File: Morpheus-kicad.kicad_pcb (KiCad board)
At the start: 2 copper layers, 64 parts, among them J1 Conn_02x03_Odd_Even, J2 Conn_02x03_Odd_Even, J3 Conn_02x03_Odd_Even, J4 Conn_02x03_Odd_Even, J5 Conn_02x05_Counter_Clockwise, Q1 IRLZ44N, Q2 IRLB3034PBF, Q3 IRLZ44N, U1 Pololu Driver, U2 Pololu Driver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

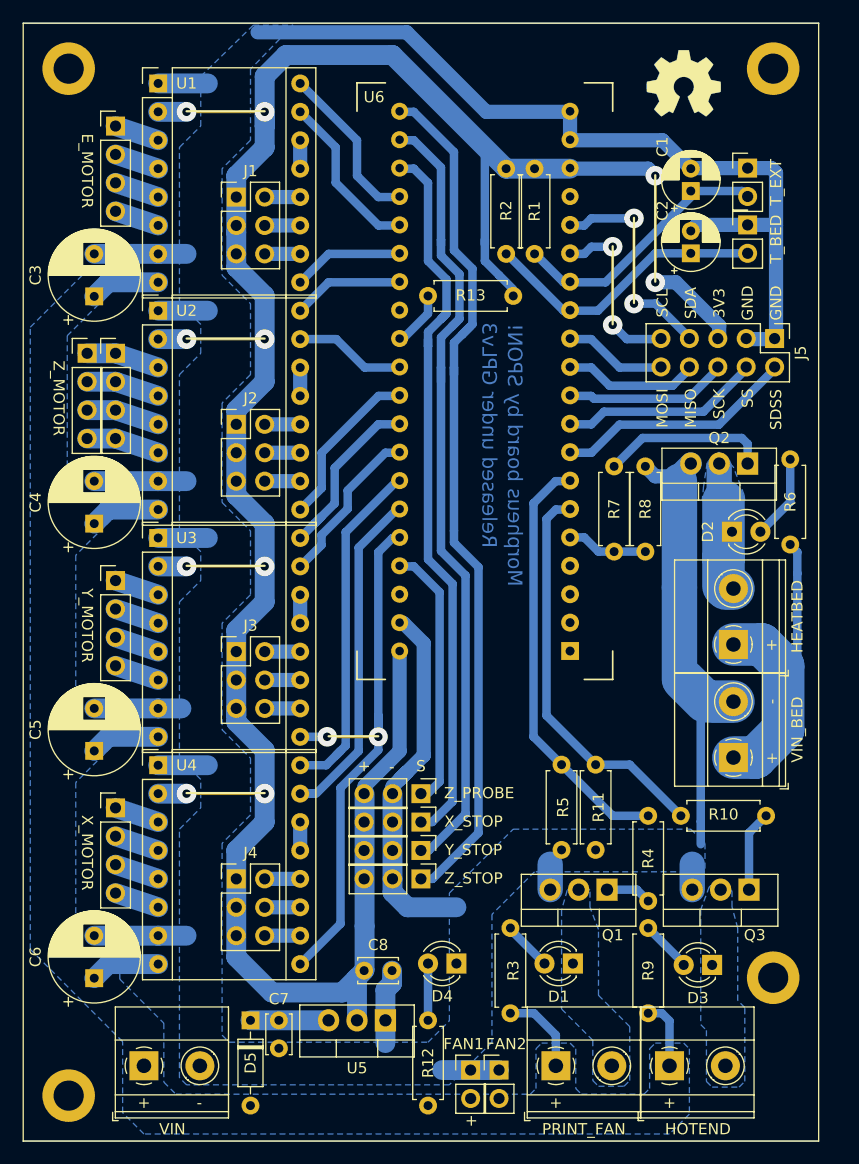
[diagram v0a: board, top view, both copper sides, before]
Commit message: Add reverse current protection
Added a 1N4007 or similar diode to protect from reverse current. Bear in mind that, without a fuse, it will just burn and let current pass again, damaging components.
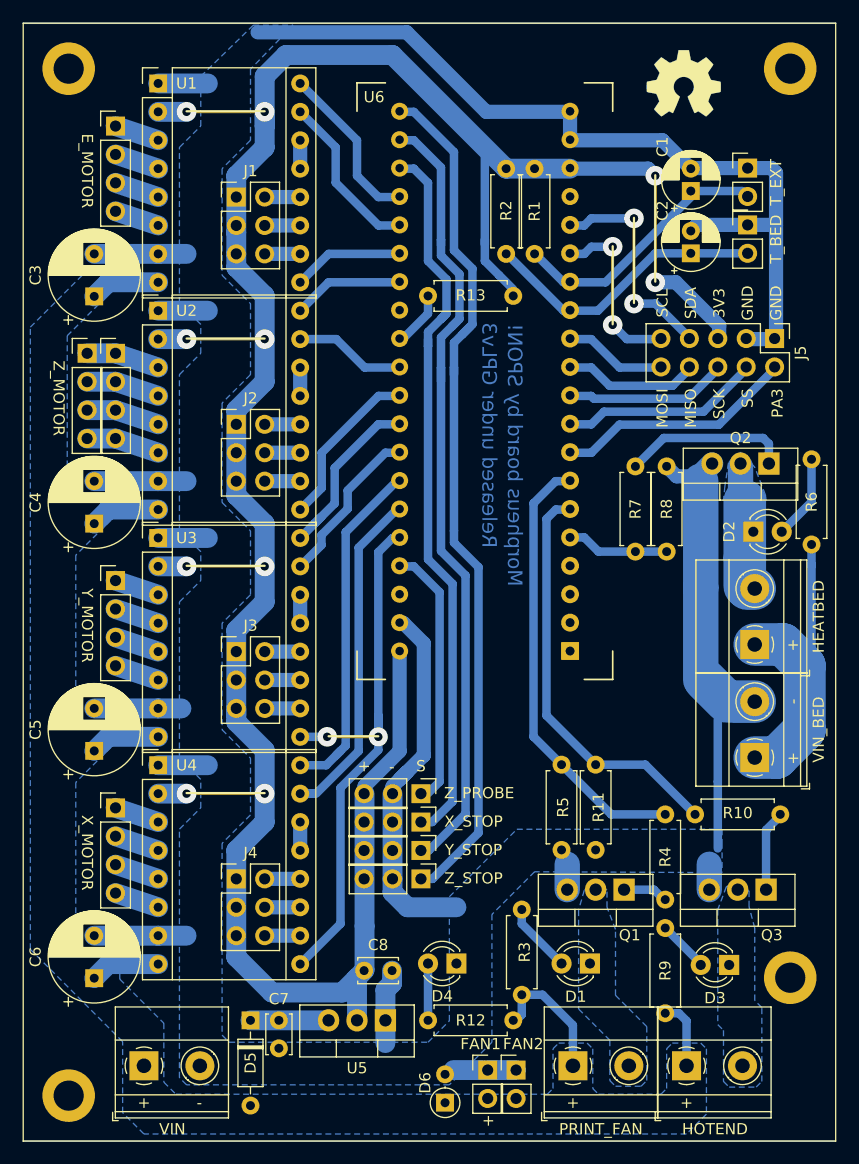
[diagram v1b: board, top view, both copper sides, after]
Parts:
- added D6: 1N4007, Diode_THT:D_DO-35_SOD27_P2.54mm_Vertical_AnodeUp, F.Cu at (73.9, 126.7)
- moved R3 1.94 mm to (80.8, 109.5)
- moved D2 1.91 mm to (101.5, 75.7)
- moved HEATBED1 1.91 mm to (101.6, 85.8)
- moved Q2 1.91 mm to (102.9, 69.6)
- moved R6 1.91 mm to (106.7, 69.2)
- moved R7 1.91 mm to (90.9, 69.8)
- moved R8 1.91 mm to (93.7, 69.8)
- moved VIN_BED1 1.91 mm to (101.6, 95.9)
- moved R4 1.53 mm to (93.6, 108.6)
- moved D1 1.52 mm to (86.9, 114.3)
- moved FAN1 1.52 mm to (77.7, 123.8)
- moved FAN2 1.52 mm to (80.3, 123.8)
- moved HOTEND1 1.52 mm to (95.5, 123.4)
- moved PRINT_FAN1 1.52 mm to (85.3, 123.4)
- moved Q1 1.52 mm to (89.9, 107.7)
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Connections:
- net SDSS renamed PA3
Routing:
- net +12V: track 38.5 -> 43.3 mm
- net (no net): track 142.2 -> 145.3 mm
- net Net-(D1-Pad2): track 4.33 -> 6.30 mm
- net HEATER_BED: track 7.26 -> 9.16 mm
- net PRINT_FAN: track 38.1 -> 39.6 mm
- net HOTEND: track 35.8 -> 37.0 mm
- net +12P: track 26.9 -> 26.0 mm
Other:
- board text added: "PA3"
- board text removed: "SDSS"

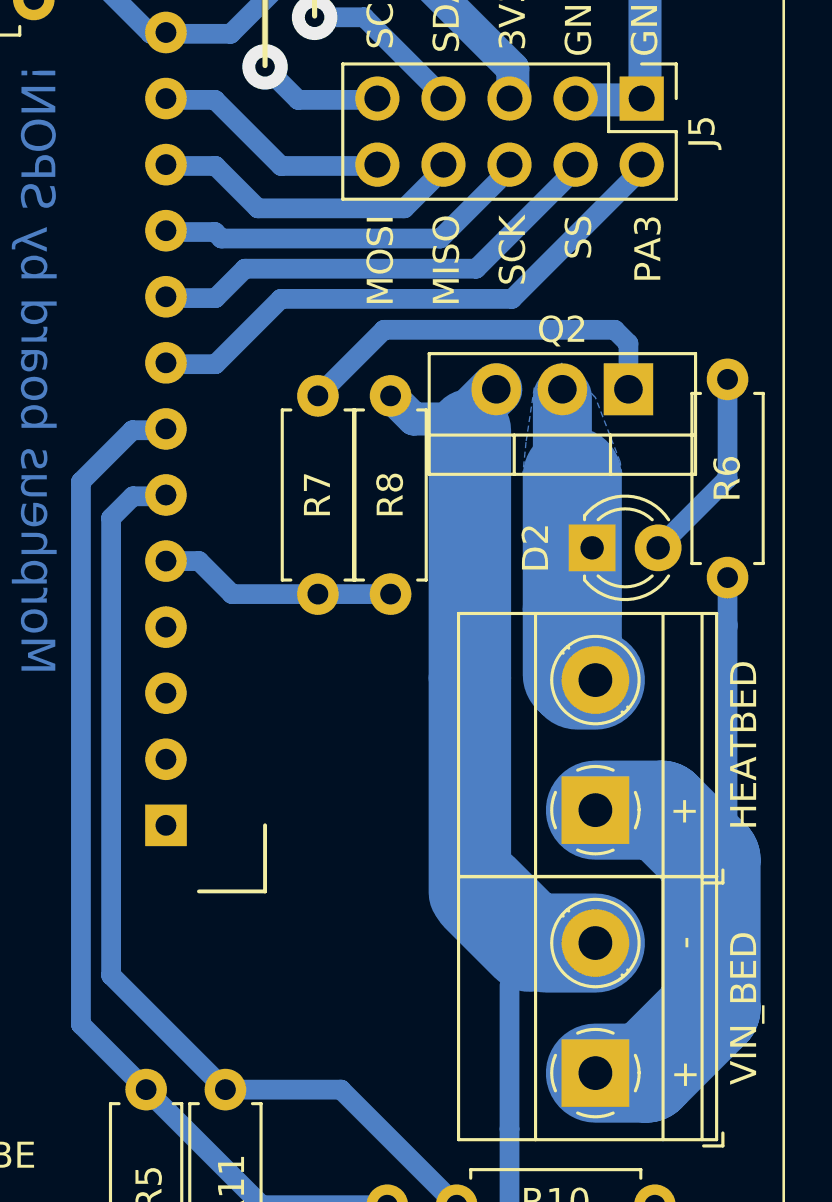
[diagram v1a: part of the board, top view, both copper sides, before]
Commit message: Add header
Added a header for the unused pins, just to make them usable.
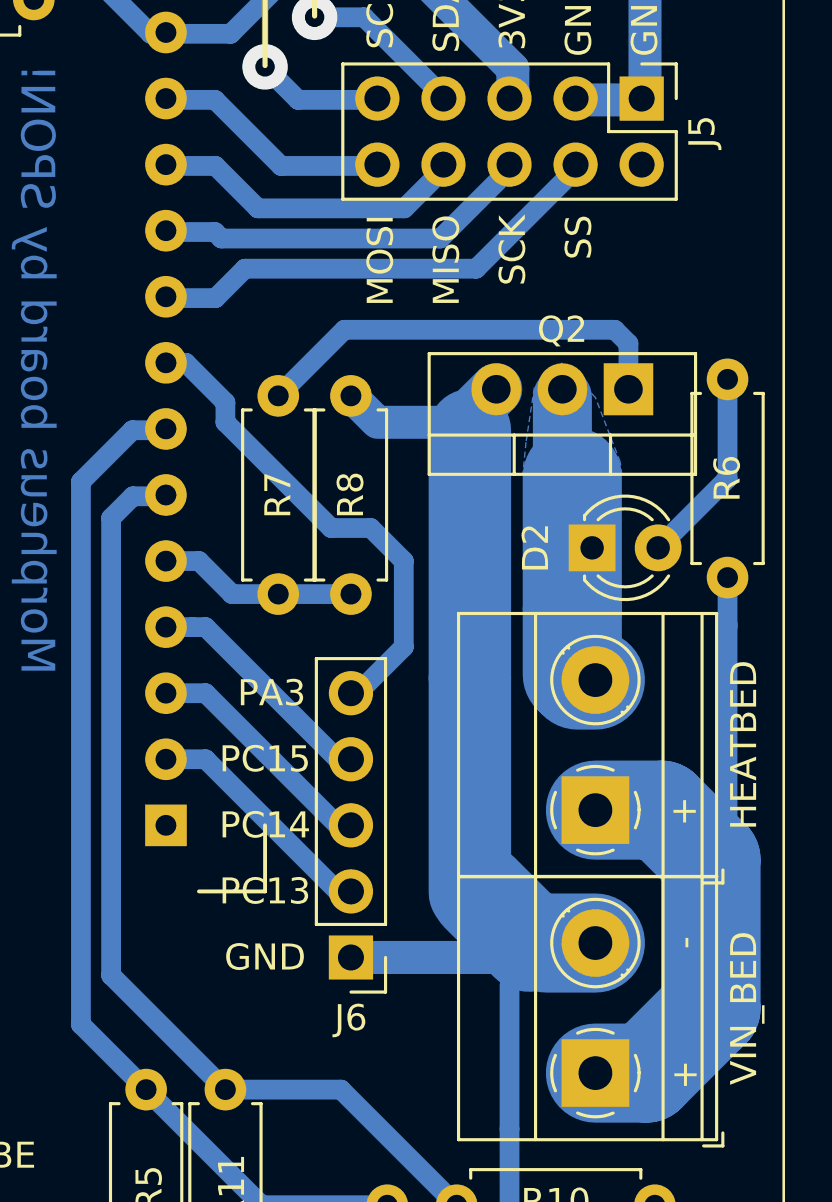
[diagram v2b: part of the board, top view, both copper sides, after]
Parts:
- added J6: Conn_01x05, Connector_PinHeader_2.54mm:PinHeader_1x05_P2.54mm_Vertical, F.Cu at (92.2, 91.4)
- moved R7 1.52 mm to (89.4, 69.8)
- moved R8 1.52 mm to (92.2, 69.8)
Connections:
- J5 pad 2: PA3 -> Net-(J5-Pad2)
- U6 pad 2: Net-(U6-Pad2) -> PC13
- U6 pad 3: Net-(U6-Pad3) -> PC14
- U6 pad 4: Net-(U6-Pad4) -> PC15
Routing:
- net PC15: track 0.00 -> 9.07 mm
- net PC14: track 0.00 -> 9.07 mm
- net PC13: track 0.00 -> 8.96 mm
- net GND: track 216.9 -> 223.9 mm
- net PA3: track 21.6 -> 18.9 mm
- net HEATER_BED: track 9.16 -> 7.64 mm
- net Net-(Q2-Pad1): track 15.0 -> 16.5 mm
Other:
- board text added: "PC13"
- board text added: "PC14"
- board text added: "PC15"
